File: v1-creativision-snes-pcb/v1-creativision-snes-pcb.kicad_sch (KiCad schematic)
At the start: 6 parts, among them J1 Conn_01x10_Pin, J2 Conn_01x10_Pin, J3 Power Entry, J4 PS/2 Keyboard, J5 SNES, U1 Pico

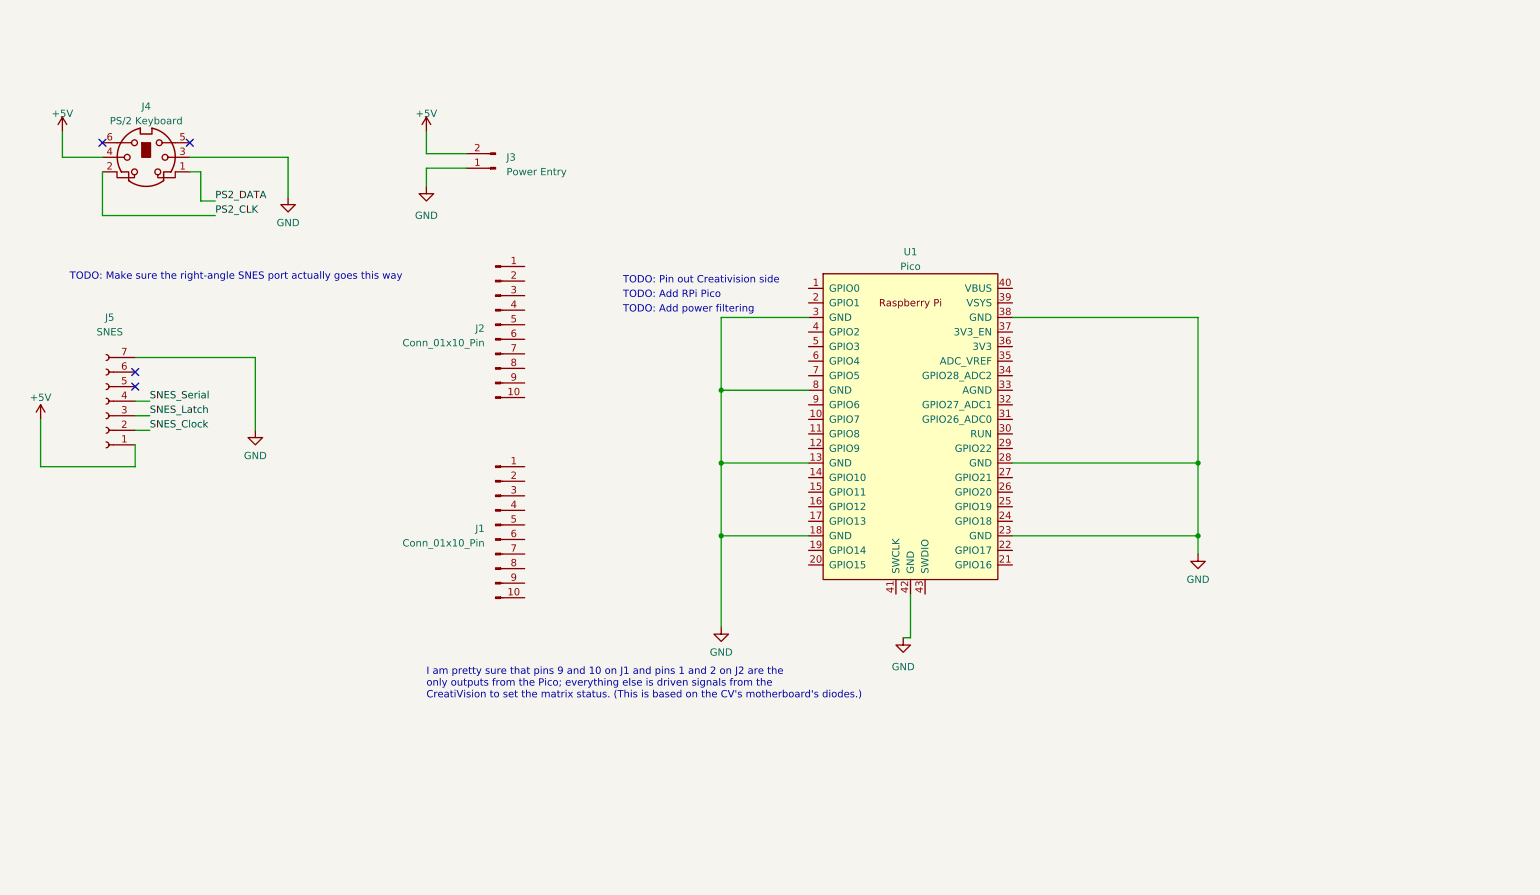
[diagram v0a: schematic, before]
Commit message: Wired up connectors to RPi Pico, still TBD on how to do 'shorting'
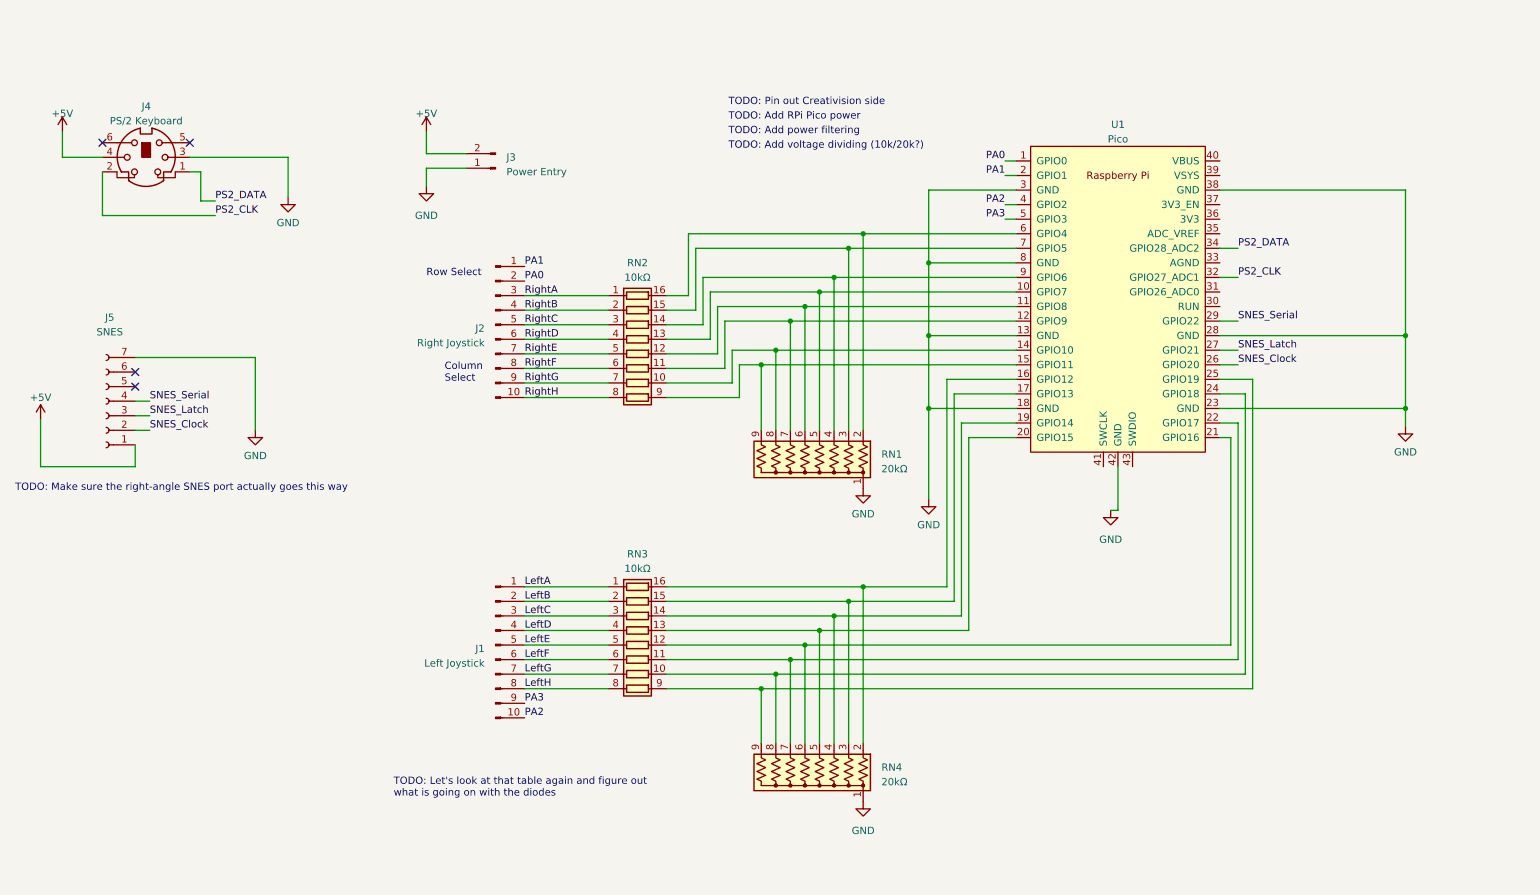
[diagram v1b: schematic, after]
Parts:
- added RN1, RN4: 20kΩ, Resistor_THT:R_Array_SIP9, symbol Device:R_Network08_US
- added RN2, RN3: 10kΩ, symbol Device:R_Pack08
- J1: value Conn_01x10_Pin -> Left Joystick
- J2: value Conn_01x10_Pin -> Right Joystick
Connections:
- net GND: now also RN1.1 (common), RN4.1 (common)
- net PS2_CLK: now also U1.32 (GPIO27_ADC1)
- net PS2_DATA: now also U1.34 (GPIO28_ADC2)
- net SNES_Clock: now also U1.26 (GPIO20)
- net SNES_Latch: now also U1.27 (GPIO21)
- net SNES_Serial: now also U1.29 (GPIO22)
- net PA1: now reaches J2.1 (Pin_1)
- net PA1: now also U1.2 (GPIO1)
- net RightH: now reaches J2.10 (Pin_10)
- net RightH: now also RN2.8 (R8.1)
- net PA0: now reaches J2.2 (Pin_2)
- net PA0: now also U1.1 (GPIO0)
- net RightA: now reaches J2.3 (Pin_3)
- net RightA: now also RN2.1 (R1.1)
- net RightB: now reaches J2.4 (Pin_4)
- net RightB: now also RN2.2 (R2.1)
- net RightC: now reaches J2.5 (Pin_5)
- net RightC: now also RN2.3 (R3.1)
- net RightD: now reaches J2.6 (Pin_6)
- net RightD: now also RN2.4 (R4.1)
- net RightE: now reaches J2.7 (Pin_7)
- net RightE: now also RN2.5 (R5.1)
- net RightF: now reaches J2.8 (Pin_8)
- net RightF: now also RN2.6 (R6.1)
- net RightG: now reaches J2.9 (Pin_9)
- net RightG: now also RN2.7 (R7.1)
- net LeftA: now reaches J1.1 (Pin_1)
- net LeftA: now also RN3.1 (R1.1)
- net PA2: now reaches J1.10 (Pin_10)
- net PA2: now also U1.4 (GPIO2)
- net LeftB: now reaches J1.2 (Pin_2)
- net LeftB: now also RN3.2 (R2.1)
- net LeftC: now reaches J1.3 (Pin_3)
- net LeftC: now also RN3.3 (R3.1)
- net LeftD: now reaches J1.4 (Pin_4)
- net LeftD: now also RN3.4 (R4.1)
- net LeftE: now reaches J1.5 (Pin_5)
- net LeftE: now also RN3.5 (R5.1)
- net LeftF: now reaches J1.6 (Pin_6)
- net LeftF: now also RN3.6 (R6.1)
- net LeftG: now reaches J1.7 (Pin_7)
- net LeftG: now also RN3.7 (R7.1)
- net LeftH: now reaches J1.8 (Pin_8)
- net LeftH: now also RN3.8 (R8.1)
- net PA3: now reaches J1.9 (Pin_9)
- net PA3: now also U1.5 (GPIO3)
- net at U1.10 (GPIO7): now also RN1.5 (R4), RN2.13 (R4.2)
- net at U1.11 (GPIO8): now also RN1.6 (R5), RN2.12 (R5.2)
- net at U1.12 (GPIO9): now also RN1.7 (R6), RN2.11 (R6.2)
- net at U1.14 (GPIO10): now also RN1.8 (R7), RN2.10 (R7.2)
- net at U1.15 (GPIO11): now also RN1.9 (R8), RN2.9 (R8.2)
- net at U1.16 (GPIO12): now also RN3.16 (R1.2), RN4.2 (R1)
- net at U1.17 (GPIO13): now also RN3.15 (R2.2), RN4.3 (R2)
- net at U1.19 (GPIO14): now also RN3.14 (R3.2), RN4.4 (R3)
- net at U1.20 (GPIO15): now also RN3.13 (R4.2), RN4.5 (R4)
- net at U1.21 (GPIO16): now also RN3.12 (R5.2), RN4.6 (R5)
- net at U1.22 (GPIO17): now also RN3.11 (R6.2), RN4.7 (R6)
- net at U1.24 (GPIO18): now also RN3.10 (R7.2), RN4.8 (R7)
- net at U1.25 (GPIO19): now also RN3.9 (R8.2), RN4.9 (R8)
- net at U1.6 (GPIO4): now also RN1.2 (R1), RN2.16 (R1.2)
- net at U1.7 (GPIO5): now also RN1.3 (R2), RN2.15 (R2.2)
- net at U1.9 (GPIO6): now also RN1.4 (R3), RN2.14 (R3.2)
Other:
- note added: "Column Select"
- note added: "Row Select"
- note added: "TODO: Add RPi Pico power"
- note added: "TODO: Add voltage dividing (10k/20k?)"
- note added: "TODO: Let's look at that table again and figure out what is going on with the diodes"
- note removed: "I am pretty sure that pins 9 and 10 on J1 and pins 1 and 2 on J2 are the only outputs from the Pico; everything else is driven signals from the CreatiVision to set the matrix status. (This is based on the CV's motherboard's diodes.)"
- note removed: "TODO: Add RPi Pico"
- moved on the sheet: J1, U1

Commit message: Power pico, add reset button for pico
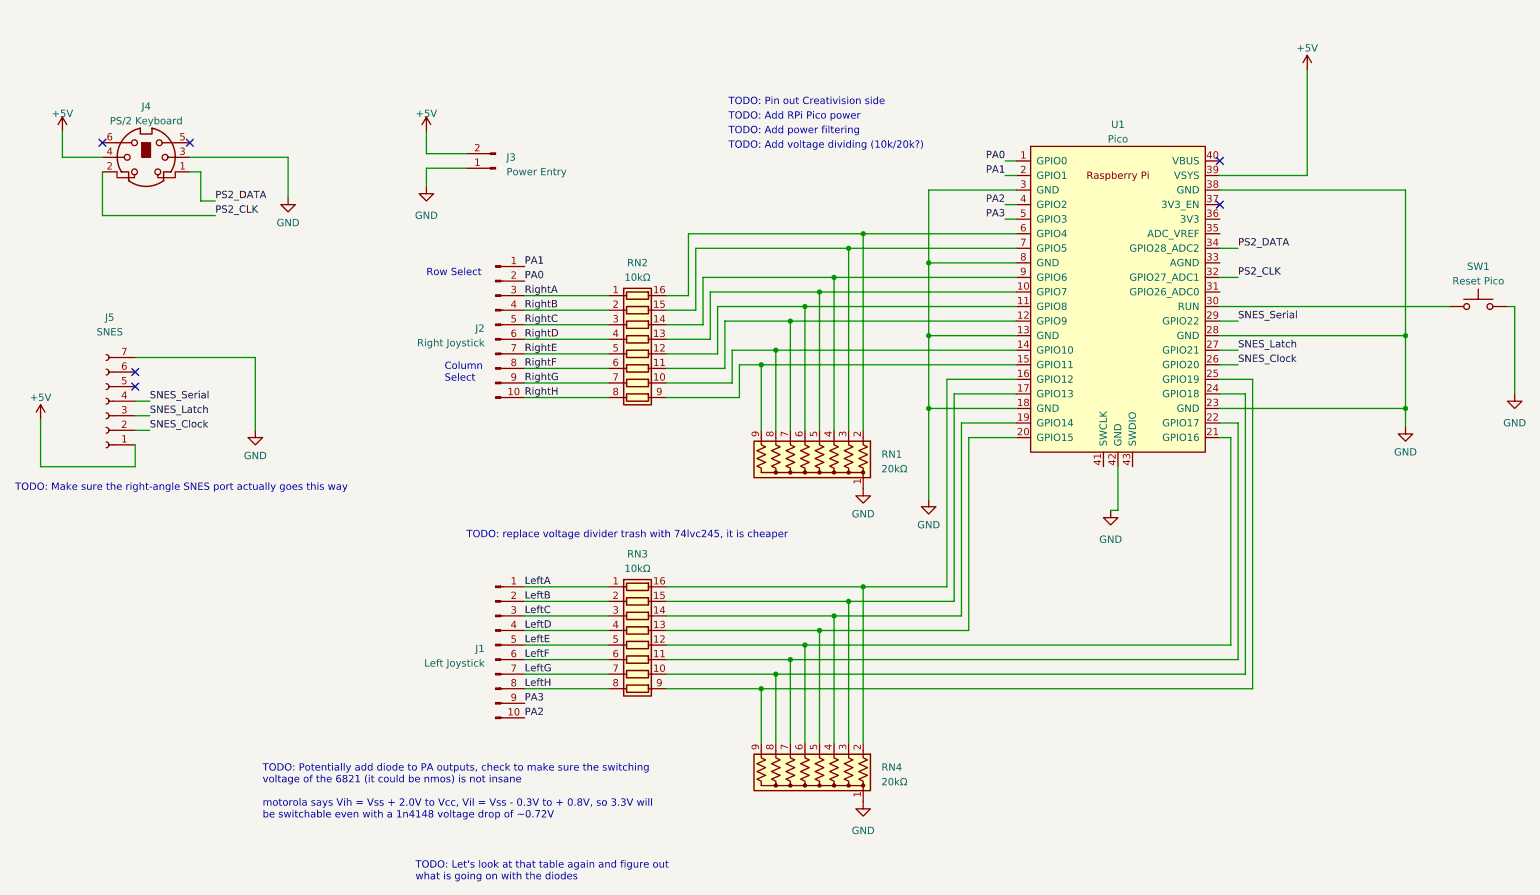
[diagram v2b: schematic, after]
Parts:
- added SW1: Reset Pico, Button_Switch_THT:SW_PUSH_6mm, symbol Switch:SW_Push
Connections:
- net +5V: now also U1.39 (VSYS)
- net GND: now also SW1.2
- net at U1.30 (RUN): now also SW1.1
- no-connect marks 4 -> 6
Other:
- note added: "TODO: Potentially add diode to PA outputs, check to make sure the switching voltage of the 6821 (it could be nmos) is not insane motorola says Vih = Vss + 2.0V to Vcc, Vil = Vss - 0.3V to + 0.8V, so 3.3V will be switchable even with a 1n4148 voltage drop of ~0.72V"
- note added: "TODO: replace voltage divider trash with 74lvc245, it is cheaper"
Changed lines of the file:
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@@
   (no_connect (at 34.29 89.535))
   (no_connect (at 28.575 46.99))
+  (no_connect (at 223.52 57.785))
   (no_connect (at 34.29 86.995))
+  (no_connect (at 223.52 50.165))
   (no_connect (at 43.815 46.99))
   (wire (pts (xy 186.055 50.165) (xy 187.96 50.165))
@@
     (stroke (width 0) (type default))
   )
+  (wire (pts (xy 263.525 75.565) (xy 223.52 75.565))
+    (stroke (width 0) (type default))
+  )
   (wire (pts (xy 255.905 55.245) (xy 223.52 55.245))
     (stroke (width 0) (type default))
@@
     (stroke (width 0) (type default))
   )
+  (wire (pts (xy 238.76 34.29) (xy 238.76 52.705))
+    (stroke (width 0) (type default))
+  )
   (wire (pts (xy 138.43 88.9) (xy 138.43 83.185))
     (stroke (width 0) (type default))
@@
     (stroke (width 0) (type default))
   )
+  (wire (pts (xy 238.76 52.705) (xy 223.52 52.705))
+    (stroke (width 0) (type default))
+  )
   (wire (pts (xy 255.905 96.52) (xy 255.905 93.345))
     (stroke (width 0) (type default))
@@
     (stroke (width 0) (type default))
   )
+  (wire (pts (xy 273.685 75.565) (xy 274.955 75.565))
+    (stroke (width 0) (type default))
+  )
   (wire (pts (xy 255.905 80.645) (xy 255.905 93.345))
     (stroke (width 0) (type default))
@@
   )
   (wire (pts (xy 179.705 98.425) (xy 187.96 98.425))
+    (stroke (width 0) (type default))
+  )
+  (wire (pts (xy 274.955 75.565) (xy 274.955 90.805))
     (stroke (width 0) (type default))
   )
@@
     (effects (font (size 1.27 1.27)) (justify left bottom))
   )
+  (text "TODO: Potentially add diode to PA outputs, check to make sure the switching\nvoltage of the 6821 (it could be nmos) is not insane\n\nmotorola says Vih = Vss + 2.0V to Vcc, Vil = Vss - 0.3V to + 0.8V, so 3.3V will\nbe switchable even with a 1n4148 voltage drop of ~0.72V"
+    (at 56.515 165.1 0)
+    (effects (font (size 1.27 1.27)) (justify left bottom))
+  )
   (text "TODO: Add power filtering" (at 137.795 45.72 0)
     (effects (font (size 1.27 1.27)) (justify left bottom))
   )
+  (text "TODO: replace voltage divider trash with 74lvc245, it is cheaper"
+    (at 92.075 116.205 0)
+    (effects (font (size 1.27 1.27)) (justify left bottom))
+  )
   (text "TODO: Let's look at that table again and figure out\nwhat is going on with the diodes"
-    (at 79.375 161.29 0)
+    (at 83.185 175.895 0)
     (effects (font (size 1.27 1.27)) (justify left bottom))
   )
@@
         (path "/3b2d64f4-47e7-4300-b1e6-31021f3d1a36"
           (reference "#PWR01") (unit 1)
+        )
+      )
+    )
+  )
+  (symbol (lib_id "Switch:SW_Push") (at 268.605 75.565 0) (unit 1)
+    (in_bom yes) (on_board yes) (dnp no) (fields_autoplaced)
+    (property "Reference" "SW1" (at 268.605 68.58 0)
+      (effects (font (size 1.27 1.27)))
+    )
+    (property "Value" "Reset Pico" (at 268.605 71.12 0)
+      (effects (font (size 1.27 1.27)))
+    )
+    (property "Footprint" "Button_Switch_THT:SW_PUSH_6mm" (at 268.605 70.485 0)
+      (effects (font (size 1.27 1.27)) hide)
+    )
+    (property "Datasheet" "~" (at 268.605 70.485 0)
+      (effects (font (size 1.27 1.27)) hide)
+    )
+    (pin "1")
+    (pin "2")
+    (instances
+      (project "v1-creativision-snes-pcb"
+        (path "/3b2d64f4-47e7-4300-b1e6-31021f3d1a36"
+          (reference "SW1") (unit 1)
+        )
+      )
+    )
+  )
+  (symbol (lib_id "power:+5V") (at 238.76 34.29 0) (unit 1)
+    (in_bom yes) (on_board yes) (dnp no) (fields_autoplaced)
+    (property "Reference" "#PWR013" (at 238.76 38.1 0)
+      (effects (font (size 1.27 1.27)) hide)
+    )
+    (property "Value" "+5V" (at 238.76 30.48 0)
+      (effects (font (size 1.27 1.27)))
+    )
+    (property "Footprint" "" (at 238.76 34.29 0)
+      (effects (font (size 1.27 1.27)) hide)
+    )
+    (property "Datasheet" "" (at 238.76 34.29 0)
+      (effects (font (size 1.27 1.27)) hide)
+    )
+    (pin "1")
+    (instances
+      (project "v1-creativision-snes-pcb"
+        (path "/3b2d64f4-47e7-4300-b1e6-31021f3d1a36"
+          (reference "#PWR013") (unit 1)
         )
       )
@@
         )
       )
+    )
+  )
+  (symbol (lib_id "power:GND") (at 274.955 90.805 0) (unit 1)
+    (in_bom yes) (on_board yes) (dnp no) (fields_autoplaced)
+    (property "Reference" "#PWR012" (at 274.955 97.155 0)
+      (effects (font (size 1.27 1.27)) hide)
+    )
+    (property "Value" "GND" (at 274.955 95.885 0)
+      (effects (font (size 1.27 1.27)))
+    )
+    (property "Footprint" "" (at 274.955 90.805 0)
+      (effects (font (size 1.27 1.27)) hide)
+    )
+    (property "Datasheet" "" (at 274.955 90.805 0)
+      (effects (font (size 1.27 1.27)) hide)
+    )
+    (pin "1")
+    (instances
+      (project "v1-creativision-snes-pcb"
+        (path "/3b2d64f4-47e7-4300-b1e6-31021f3d1a36"
+          (reference "#PWR012") (unit 1)
+        )
+      )
